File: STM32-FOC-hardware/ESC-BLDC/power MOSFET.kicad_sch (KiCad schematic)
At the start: 60 parts, among them P1 XT30PW-M, P2 XT30PW-M, P3 DP-01, P4 DP-01, P5 DP-01, Q1 FDMS8820, Q2 FDMS8820, Q3 FDMS8820, Q4 FDMS8820, Q5 FDMS8820, Q6 FDMS8820, U2 LP2985-33DBVR

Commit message: Audit sourcing symmetry and divider choices
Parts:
- R25, R26, R27: MPN 0402WGF2201TCE -> 0402WGF2001TCE
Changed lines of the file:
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@@
 			)
 		)
-		(property "MPN" "0402WGF2201TCE"
+		(property "MPN" "0402WGF2001TCE"
 			(at 256.54 149.0472 0)
 			(hide yes)
@@
 			)
 		)
-		(property "MPN" "0402WGF2201TCE"
+		(property "MPN" "0402WGF2001TCE"
 			(at 71.12 149.0472 0)
 			(hide yes)
@@
 			)
 		)
-		(property "MPN" "0402WGF2201TCE"
+		(property "MPN" "0402WGF2001TCE"
 			(at 162.56 149.0472 0)
 			(hide yes)

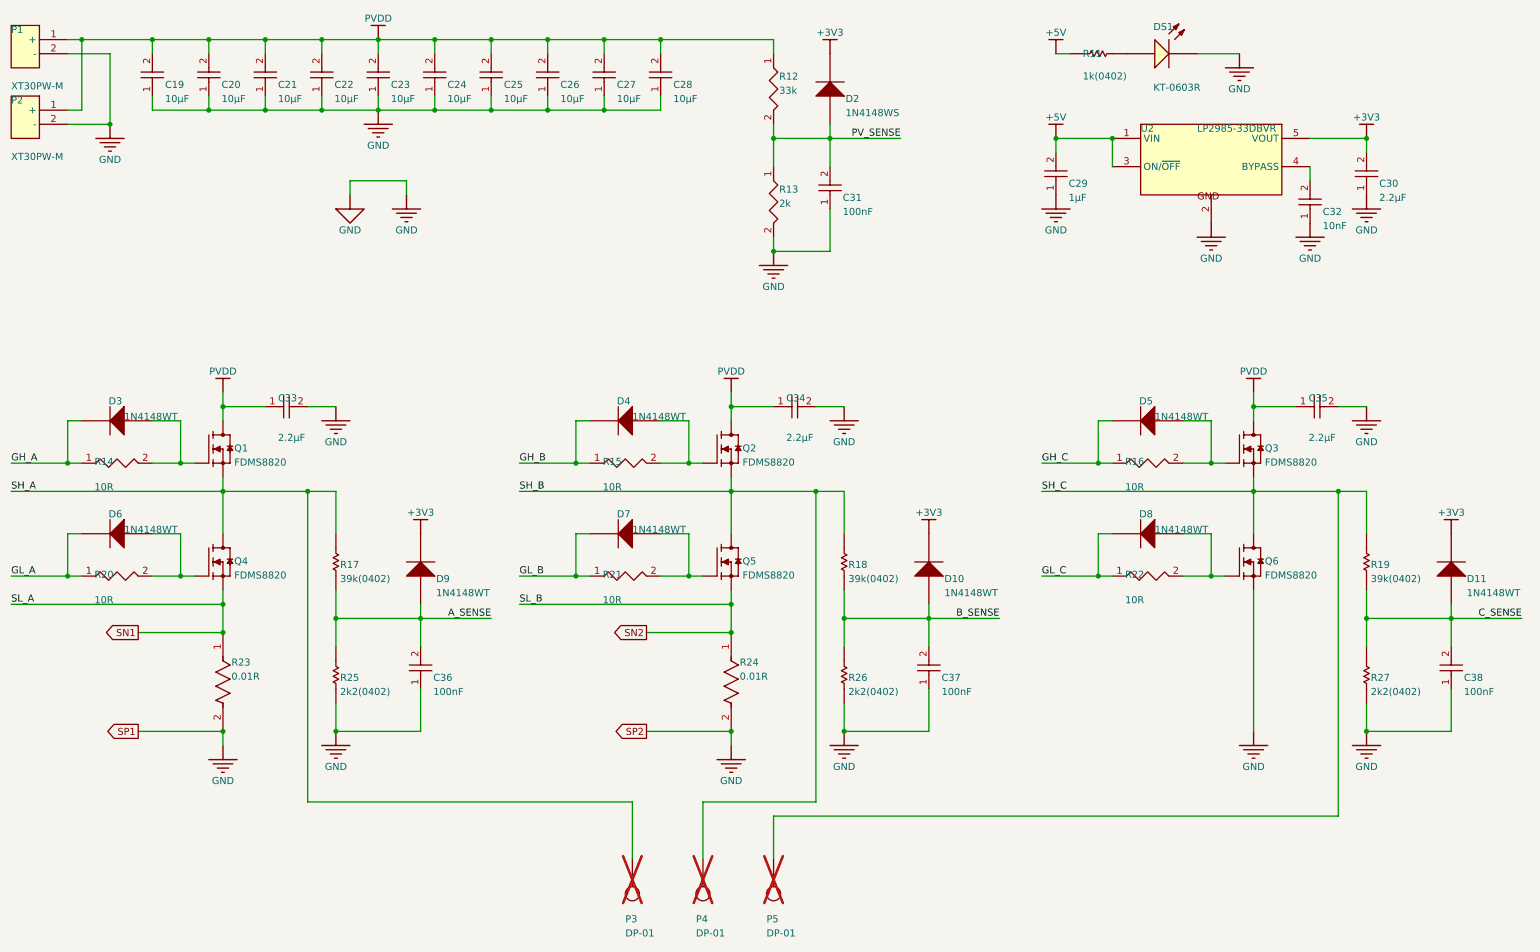
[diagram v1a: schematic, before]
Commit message: Apply schematic cleanup and sourcing todo
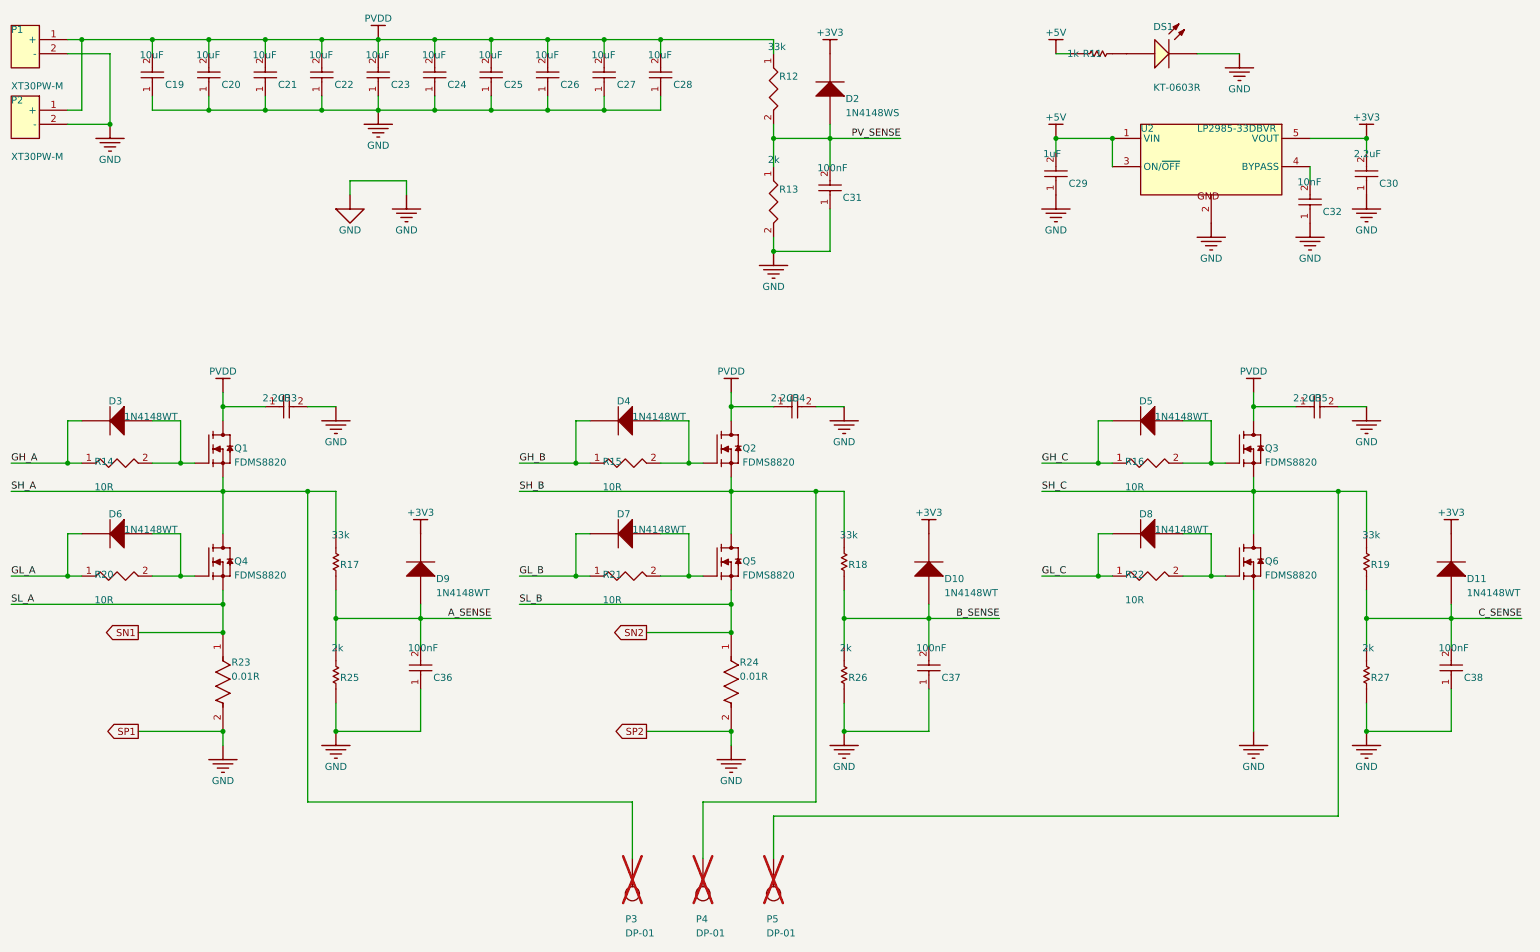
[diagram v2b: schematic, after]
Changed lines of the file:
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@@
 		(property "Value" "33k"
 			(at 70.358 120.5992 0)
-			(hide yes)
 			(show_name no)
 			(do_not_autoplace no)
@@
 		(property "ALTIUM_VALUE" "39k(0402)"
 			(at 71.882 128.4732 0)
+			(hide yes)
 			(show_name no)
 			(do_not_autoplace no)
@@
 		(property "Value" "1uF"
 			(at 198.374 52.0192 0)
-			(hide yes)
 			(show_name no)
 			(do_not_autoplace no)
@@
 		(property "ALTIUM_VALUE" "1µF"
 			(at 202.946 59.8932 0)
+			(hide yes)
 			(show_name no)
 			(do_not_autoplace no)
@@
 		(property "Value" "10uF"
 			(at 117.094 34.2392 0)
-			(hide yes)
 			(show_name no)
 			(do_not_autoplace no)
@@
 		(property "ALTIUM_VALUE" "10µF"
 			(at 121.666 42.1132 0)
+			(hide yes)
 			(show_name no)
 			(do_not_autoplace no)
@@
 		(property "Value" "10uF"
 			(at 56.134 34.2392 0)
-			(hide yes)
 			(show_name no)
 			(do_not_autoplace no)
@@
 		(property "ALTIUM_VALUE" "10µF"
 			(at 60.706 42.1132 0)
+			(hide yes)
 			(show_name no)
 			(do_not_autoplace no)
@@
 		(property "Value" "10R"
 			(at 27.686 111.9632 90)
-			(hide yes)
 			(show_name no)
 			(do_not_autoplace no)
@@
 		(property "ALTIUM_VALUE" "10R"
 			(at 27.686 111.9632 90)
+			(hide yes)
 			(show_name no)
 			(do_not_autoplace no)
@@
 		(property "Value" "33k"
 			(at 148.844 34.2392 0)
-			(hide yes)
 			(show_name no)
 			(do_not_autoplace no)
@@
 		(property "ALTIUM_VALUE" "33k"
 			(at 150.876 42.1132 0)
+			(hide yes)
 			(show_name no)
 			(do_not_autoplace no)
@@
 		(property "Value" "2k"
 			(at 255.778 140.9192 0)
-			(hide yes)
 			(show_name no)
 			(do_not_autoplace no)
@@
 		(property "ALTIUM_VALUE" "2k2(0402)"
 			(at 257.302 148.7932 0)
+			(hide yes)
 			(show_name no)
 			(do_not_autoplace no)
@@
 		(property "Value" "10uF"
 			(at 66.294 34.2392 0)
-			(hide yes)
 			(show_name no)
 			(do_not_autoplace no)
@@
 		(property "ALTIUM_VALUE" "10µF"
 			(at 70.866 42.1132 0)
+			(hide yes)
 			(show_name no)
 			(do_not_autoplace no)
@@
 		(property "Value" "100nF"
 			(at 175.514 140.9192 0)
-			(hide yes)
 			(show_name no)
 			(do_not_autoplace no)
@@
 		(property "ALTIUM_VALUE" "100nF"
 			(at 180.086 148.7932 0)
+			(hide yes)
 			(show_name no)
 			(do_not_autoplace no)
@@
 		(property "Value" "2.2uF"
 			(at 254.254 52.0192 0)
-			(hide yes)
 			(show_name no)
 			(do_not_autoplace no)
@@
 		(property "ALTIUM_VALUE" "2.2µF"
 			(at 258.826 59.8932 0)
+			(hide yes)
 			(show_name no)
 			(do_not_autoplace no)
@@
 		(property "Value" "10uF"
 			(at 96.774 34.2392 0)
-			(hide yes)
 			(show_name no)
 			(do_not_autoplace no)
@@
 		(property "ALTIUM_VALUE" "10µF"
 			(at 101.346 42.1132 0)
+			(hide yes)
 			(show_name no)
 			(do_not_autoplace no)
@@
 		(property "Value" "10uF"
 			(at 106.934 34.2392 0)
-			(hide yes)
 			(show_name no)
 			(do_not_autoplace no)
@@
 		(property "ALTIUM_VALUE" "10µF"
 			(at 111.506 42.1132 0)
+			(hide yes)
 			(show_name no)
 			(do_not_autoplace no)
@@
 		(property "Value" "10uF"
 			(at 127.254 34.2392 0)
-			(hide yes)
 			(show_name no)
 			(do_not_autoplace no)
@@
 		(property "ALTIUM_VALUE" "10µF"
 			(at 131.826 42.1132 0)
+			(hide yes)
 			(show_name no)
 			(do_not_autoplace no)
@@
 		(property "Value" "2k"
 			(at 70.358 140.9192 0)
-			(hide yes)
 			(show_name no)
 			(do_not_autoplace no)
@@
 		(property "ALTIUM_VALUE" "2k2(0402)"
 			(at 71.882 148.7932 0)
+			(hide yes)
 			(show_name no)
 			(do_not_autoplace no)
@@
 		(property "Value" "1k"
 			(at 202.692 33.9852 90)
-			(hide yes)
 			(show_name no)
 			(do_not_autoplace no)
@@
 		(property "ALTIUM_VALUE" "1k(0402)"
 			(at 205.486 38.0492 90)
+			(hide yes)
 			(show_name no)
 			(do_not_autoplace no)
@@
 		(property "Value" "10uF"
 			(at 45.974 34.2392 0)
-			(hide yes)
 			(show_name no)
 			(do_not_autoplace no)
@@
 		(property "ALTIUM_VALUE" "10µF"
 			(at 50.546 42.1132 0)
+			(hide yes)
 			(show_name no)
 			(do_not_autoplace no)
@@
 		(property "Value" "2k"
 			(at 148.844 54.5592 0)
-			(hide yes)
 			(show_name no)
 			(do_not_autoplace no)
@@
 		(property "ALTIUM_VALUE" "2k"
 			(at 150.876 62.4332 0)
+			(hide yes)
 			(show_name no)
 			(do_not_autoplace no)
@@
 		(property "Value" "100nF"
 			(at 84.074 140.9192 0)
-			(hide yes)
 			(show_name no)
 			(do_not_autoplace no)
@@
 		(property "ALTIUM_VALUE" "100nF"
 			(at 88.646 148.7932 0)
+			(hide yes)
 			(show_name no)
 			(do_not_autoplace no)
@@
 		(property "Value" "2k"
 			(at 161.798 140.9192 0)
-			(hide yes)
 			(show_name no)
 			(do_not_autoplace no)
@@
 		(property "ALTIUM_VALUE" "2k2(0402)"
 			(at 163.322 148.7932 0)
+			(hide yes)
 			(show_name no)
 			(do_not_autoplace no)
@@
 		(property "Value" "10R"
 			(at 213.106 132.2832 90)
-			(hide yes)
 			(show_name no)
 			(do_not_autoplace no)
@@
 		(property "ALTIUM_VALUE" "10R"
 			(at 213.106 132.2832 90)
+			(hide yes)
 			(show_name no)
 			(do_not_autoplace no)
@@
 		(property "Value" "2.2uF"
 			(at 57.912 95.9612 90)
-			(hide yes)
 			(show_name no)
 			(do_not_autoplace no)
@@
 		(property "ALTIUM_VALUE" "2.2µF"
 			(at 60.706 103.0732 90)
+			(hide yes)
 			(show_name no)
 			(do_not_autoplace no)
@@
 		(property "Value" "100nF"
 			(at 157.734 54.5592 0)
-			(hide yes)
 			(show_name no)
 			(do_not_autoplace no)
@@
 		(property "ALTIUM_VALUE" "100nF"
 			(at 162.306 62.4332 0)
+			(hide yes)
 			(show_name no)
 			(do_not_autoplace no)
@@
 		(property "Value" "2.2uF"
 			(at 243.332 95.9612 90)
-			(hide yes)
 			(show_name no)
 			(do_not_autoplace no)
@@
 		(property "ALTIUM_VALUE" "2.2µF"
 			(at 246.126 103.0732 90)
+			(hide yes)
 			(show_name no)
 			(do_not_autoplace no)
@@
 		(property "Value" "10R"
 			(at 119.126 111.9632 90)
-			(hide yes)
 			(show_name no)
 			(do_not_autoplace no)
@@
 		(property "ALTIUM_VALUE" "10R"
 			(at 119.126 111.9632 90)
+			(hide yes)
 			(show_name no)
 			(do_not_autoplace no)
@@
 		(property "Value" "10uF"
 			(at 35.814 34.2392 0)
-			(hide yes)
 			(show_name no)
 			(do_not_autoplace no)
@@
 		(property "ALTIUM_VALUE" "10µF"
 			(at 40.386 42.1132 0)
+			(hide yes)
 			(show_name no)
 			(do_not_autoplace no)
@@
 		(property "Value" "33k"
 			(at 161.798 120.5992 0)
-			(hide yes)
 			(show_name no)
 			(do_not_autoplace no)
@@
 		(property "ALTIUM_VALUE" "39k(0402)"
 			(at 163.322 128.4732 0)
+			(hide yes)
 			(show_name no)
 			(do_not_autoplace no)
@@
 		(property "Value" "10uF"
 			(at 76.454 34.2392 0)
-			(hide yes)
 			(show_name no)
 			(do_not_autoplace no)
@@
 		(property "ALTIUM_VALUE" "10µF"
 			(at 81.026 42.1132 0)
+			(hide yes)
 			(show_name no)
 			(do_not_autoplace no)
@@
 		(property "Value" "10R"
 			(at 213.106 111.9632 90)
-			(hide yes)
 			(show_name no)
 			(do_not_autoplace no)
@@
 		(property "ALTIUM_VALUE" "10R"
 			(at 213.106 111.9632 90)
+			(hide yes)
 			(show_name no)
 			(do_not_autoplace no)
@@
 		(property "Value" "10R"
 			(at 119.126 132.2832 90)
-			(hide yes)
 			(show_name no)
 			(do_not_autoplace no)
@@
 		(property "ALTIUM_VALUE" "10R"
 			(at 119.126 132.2832 90)
+			(hide yes)
 			(show_name no)
 			(do_not_autoplace no)
@@
 		(property "Value" "10R"
 			(at 27.686 132.2832 90)
-			(hide yes)
 			(show_name no)
 			(do_not_autoplace no)
@@
 		(property "ALTIUM_VALUE" "10R"
 			(at 27.686 132.2832 90)
+			(hide yes)
 			(show_name no)
 			(do_not_autoplace no)
@@
 		(property "Value" "2.2uF"
 			(at 149.352 95.9612 90)
-			(hide yes)
 			(show_name no)
 			(do_not_autoplace no)
@@
 		(property "ALTIUM_VALUE" "2.2µF"
 			(at 152.146 103.0732 90)
+			(hide yes)
 			(show_name no)
 			(do_not_autoplace no)
@@
 		(property "Value" "100nF"
 			(at 269.494 140.9192 0)
-			(hide yes)
 			(show_name no)
 			(do_not_autoplace no)
@@
 		(property "ALTIUM_VALUE" "100nF"
 			(at 274.066 148.7932 0)
+			(hide yes)
 			(show_name no)
 			(do_not_autoplace no)
@@
 		(property "Value" "10nF"
 			(at 244.094 57.0992 0)
-			(hide yes)
 			(show_name no)
 			(do_not_autoplace no)
@@
 		(property "ALTIUM_VALUE" "10nF"
 			(at 248.666 64.9732 0)
+			(hide yes)
 			(show_name no)
 			(do_not_autoplace no)
@@
 		(property "Value" "10uF"
 			(at 86.614 34.2392 0)
-			(hide yes)
 			(show_name no)
 			(do_not_autoplace no)
@@
 		(property "ALTIUM_VALUE" "10µF"
 			(at 91.186 42.1132 0)
+			(hide yes)
 			(show_name no)
 			(do_not_autoplace no)
@@
 		(property "Value" "33k"
 			(at 255.778 120.5992 0)
-			(hide yes)
 			(show_name no)
 			(do_not_autoplace no)
@@
 		(property "ALTIUM_VALUE" "39k(0402)"
 			(at 257.302 128.4732 0)
+			(hide yes)
 			(show_name no)
 			(do_not_autoplace no)
